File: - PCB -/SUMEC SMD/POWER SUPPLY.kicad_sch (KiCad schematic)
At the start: 7 parts, among them U8 LM1084IS-5.0/NOPB, U9 LM1084IS-3.3/NOPB

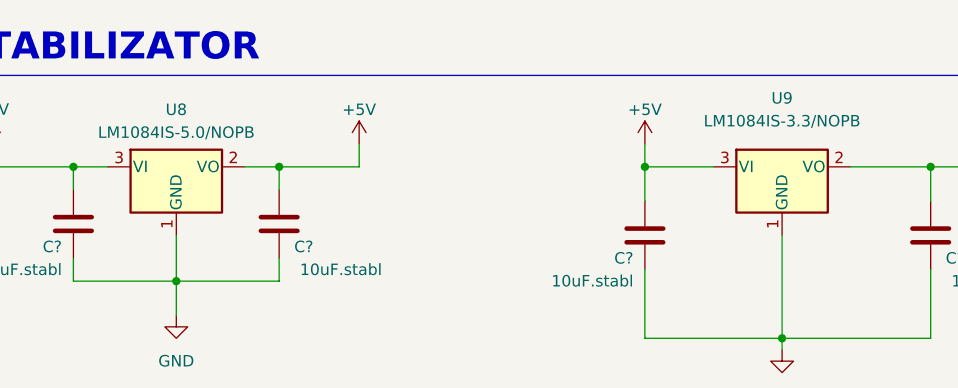
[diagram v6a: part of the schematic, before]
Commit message: Minor redesign
Distance sensor connector pin order chenged, LDO regulator heat pads added, mounting holes layout changed
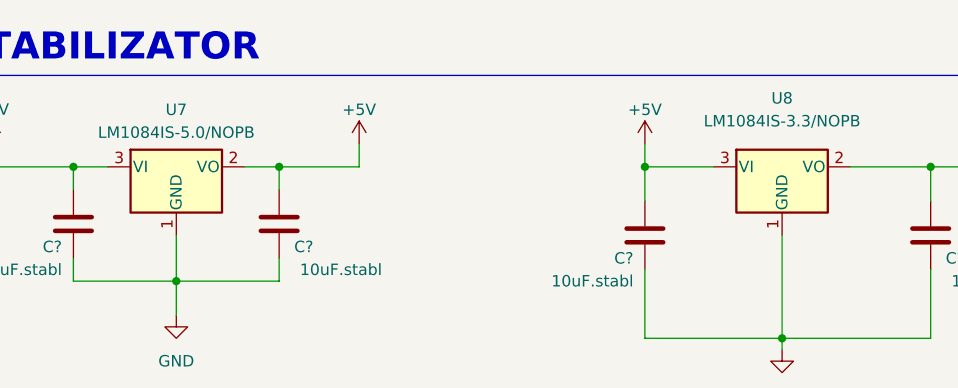
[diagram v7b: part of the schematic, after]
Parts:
- renumbered U8 to U7, U9 to U8
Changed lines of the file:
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@@
         )
         (path "/fc70a1a8-ed7c-4a0f-9b1a-f23293528385/2febd48c-c6ec-477b-ac64-6fa98a41fff0"
-          (reference "#PWR047") (unit 1)
+          (reference "#PWR048") (unit 1)
         )
       )
@@
   (symbol (lib_id "power:+5V") (at 205.74 39.37 0) (unit 1)
     (in_bom yes) (on_board yes) (dnp no) (fields_autoplaced)
-    (property "Reference" "#PWR045" (at 205.74 43.18 0)
+    (property "Reference" "#PWR046" (at 205.74 43.18 0)
       (effects (font (size 1.27 1.27)) hide)
     )
@@
       (project "sumec"
         (path "/fc70a1a8-ed7c-4a0f-9b1a-f23293528385/2febd48c-c6ec-477b-ac64-6fa98a41fff0"
-          (reference "#PWR045") (unit 1)
+          (reference "#PWR046") (unit 1)
         )
       )
@@
   (symbol (lib_id "Regulator_Linear:LM1084-3.3") (at 220.98 41.91 0) (unit 1)
     (in_bom yes) (on_board yes) (dnp no) (fields_autoplaced)
-    (property "Reference" "U9" (at 220.98 34.29 0)
+    (property "Reference" "U8" (at 220.98 34.29 0)
       (effects (font (size 1.27 1.27)))
     )
@@
       (project "sumec"
         (path "/fc70a1a8-ed7c-4a0f-9b1a-f23293528385/2febd48c-c6ec-477b-ac64-6fa98a41fff0"
-          (reference "U9") (unit 1)
+          (reference "U8") (unit 1)
         )
       )
@@
         )
         (path "/fc70a1a8-ed7c-4a0f-9b1a-f23293528385/2febd48c-c6ec-477b-ac64-6fa98a41fff0"
-          (reference "#PWR046") (unit 1)
+          (reference "#PWR047") (unit 1)
         )
       )
@@
   (symbol (lib_id "Regulator_Linear:LM1084-3.3") (at 153.67 41.91 0) (unit 1)
     (in_bom yes) (on_board yes) (dnp no) (fields_autoplaced)
-    (property "Reference" "U8" (at 153.67 35.56 0)
+    (property "Reference" "U7" (at 153.67 35.56 0)
       (effects (font (size 1.27 1.27)))
     )
@@
       (project "sumec"
         (path "/fc70a1a8-ed7c-4a0f-9b1a-f23293528385/2febd48c-c6ec-477b-ac64-6fa98a41fff0"
-          (reference "U8") (unit 1)
+          (reference "U7") (unit 1)
         )
       )
@@
         )
         (path "/fc70a1a8-ed7c-4a0f-9b1a-f23293528385/2febd48c-c6ec-477b-ac64-6fa98a41fff0"
-          (reference "#PWR042") (unit 1)
+          (reference "#PWR043") (unit 1)
         )
       )
@@
         )
         (path "/fc70a1a8-ed7c-4a0f-9b1a-f23293528385/2febd48c-c6ec-477b-ac64-6fa98a41fff0"
+          (reference "#PWR045") (unit 1)
+        )
+      )
+    )
+  )
+  (symbol (lib_id "Device:C") (at 142.24 48.26 0) (mirror y) (unit 1)
+    (in_bom yes) (on_board yes) (dnp no)
+    (property "Reference" "C?" (at 140.97 50.8 0)
+      (effects (font (size 1.27 1.27)) (justify left))
+    )
+    (property "Value" "10uF.stabl" (at 140.97 53.34 0)
+      (effects (font (size 1.27 1.27)) (justify left))
+    )
+    (property "Footprint" "Capacitor_SMD:C_1206_3216Metric_Pad1.33x1.80mm_HandSolder" (at 141.2748 52.07 0)
+      (effects (font (size 1.27 1.27)) hide)
+    )
+    (property "Datasheet" "~" (at 142.24 48.26 0)
+      (effects (font (size 1.27 1.27)) hide)
+    )
+    (pin "1")
+    (pin "2")
+    (instances
+      (project "sumec"
+        (path "/fc70a1a8-ed7c-4a0f-9b1a-f23293528385"
+          (reference "C?") (unit 1)
+        )
+        (path "/fc70a1a8-ed7c-4a0f-9b1a-f23293528385/2febd48c-c6ec-477b-ac64-6fa98a41fff0"
+          (reference "C10") (unit 1)
+        )
+      )
+    )
+  )
+  (symbol (lib_id "power:+8V") (at 133.35 39.37 0) (unit 1)
+    (in_bom yes) (on_board yes) (dnp no)
+    (property "Reference" "#PWR042" (at 133.35 43.18 0)
+      (effects (font (size 1.27 1.27)) hide)
+    )
+    (property "Value" "+8V" (at 131.3287 35.532 0)
+      (effects (font (size 1.27 1.27)) (justify left))
+    )
+    (property "Footprint" "" (at 133.35 39.37 0)
+      (effects (font (size 1.27 1.27)) hide)
+    )
+    (property "Datasheet" "" (at 133.35 39.37 0)
+      (effects (font (size 1.27 1.27)) hide)
+    )
+    (pin "1")
+    (instances
+      (project "sumec"
+        (path "/fc70a1a8-ed7c-4a0f-9b1a-f23293528385/2febd48c-c6ec-477b-ac64-6fa98a41fff0"
+          (reference "#PWR042") (unit 1)
+        )
+      )
+    )
+  )
+  (symbol (lib_id "power:+5V") (at 173.99 39.37 0) (unit 1)
+    (in_bom yes) (on_board yes) (dnp no) (fields_autoplaced)
+    (property "Reference" "#PWR044" (at 173.99 43.18 0)
+      (effects (font (size 1.27 1.27)) hide)
+    )
+    (property "Value" "+5V" (at 173.99 35.56 0)
+      (effects (font (size 1.27 1.27)))
+    )
+    (property "Footprint" "" (at 173.99 39.37 0)
+      (effects (font (size 1.27 1.27)) hide)
+    )
+    (property "Datasheet" "" (at 173.99 39.37 0)
+      (effects (font (size 1.27 1.27)) hide)
+    )
+    (pin "1")
+    (instances
+      (project "sumec"
+        (path "/fc70a1a8-ed7c-4a0f-9b1a-f23293528385/2febd48c-c6ec-477b-ac64-6fa98a41fff0"
           (reference "#PWR044") (unit 1)
         )
       )
-    )
-  )
-  (symbol (lib_id "Device:C") (at 142.24 48.26 0) (mirror y) (unit 1)
-    (in_bom yes) (on_board yes) (dnp no)
-    (property "Reference" "C?" (at 140.97 50.8 0)
-      (effects (font (size 1.27 1.27)) (justify left))
-    )
-    (property "Value" "10uF.stabl" (at 140.97 53.34 0)
-      (effects (font (size 1.27 1.27)) (justify left))
-    )
-    (property "Footprint" "Capacitor_SMD:C_1206_3216Metric_Pad1.33x1.80mm_HandSolder" (at 141.2748 52.07 0)
-      (effects (font (size 1.27 1.27)) hide)
-    )
-    (property "Datasheet" "~" (at 142.24 48.26 0)
-      (effects (font (size 1.27 1.27)) hide)
-    )
-    (pin "1")
-    (pin "2")
-    (instances
-      (project "sumec"
-        (path "/fc70a1a8-ed7c-4a0f-9b1a-f23293528385"
-          (reference "C?") (unit 1)
-        )
-        (path "/fc70a1a8-ed7c-4a0f-9b1a-f23293528385/2febd48c-c6ec-477b-ac64-6fa98a41fff0"
-          (reference "C10") (unit 1)
-        )
-      )
-    )
-  )
-  (symbol (lib_id "power:+8V") (at 133.35 39.37 0) (unit 1)
-    (in_bom yes) (on_board yes) (dnp no)
-    (property "Reference" "#PWR041" (at 133.35 43.18 0)
-      (effects (font (size 1.27 1.27)) hide)
-    )
-    (property "Value" "+8V" (at 131.3287 35.532 0)
-      (effects (font (size 1.27 1.27)) (justify left))
-    )
-    (property "Footprint" "" (at 133.35 39.37 0)
-      (effects (font (size 1.27 1.27)) hide)
-    )
-    (property "Datasheet" "" (at 133.35 39.37 0)
-      (effects (font (size 1.27 1.27)) hide)
-    )
-    (pin "1")
-    (instances
-      (project "sumec"
-        (path "/fc70a1a8-ed7c-4a0f-9b1a-f23293528385/2febd48c-c6ec-477b-ac64-6fa98a41fff0"
-          (reference "#PWR041") (unit 1)
-        )
-      )
-    )
-  )
-  (symbol (lib_id "power:+5V") (at 173.99 39.37 0) (unit 1)
-    (in_bom yes) (on_board yes) (dnp no) (fields_autoplaced)
-    (property "Reference" "#PWR043" (at 173.99 43.18 0)
-      (effects (font (size 1.27 1.27)) hide)
-    )
-    (property "Value" "+5V" (at 173.99 35.56 0)
-      (effects (font (size 1.27 1.27)))
-    )
-    (property "Footprint" "" (at 173.99 39.37 0)
-      (effects (font (size 1.27 1.27)) hide)
-    )
-    (property "Datasheet" "" (at 173.99 39.37 0)
-      (effects (font (size 1.27 1.27)) hide)
-    )
-    (pin "1")
-    (instances
-      (project "sumec"
-        (path "/fc70a1a8-ed7c-4a0f-9b1a-f23293528385/2febd48c-c6ec-477b-ac64-6fa98a41fff0"
-          (reference "#PWR043") (unit 1)
-        )
-      )
